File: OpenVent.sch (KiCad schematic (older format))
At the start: 0 parts

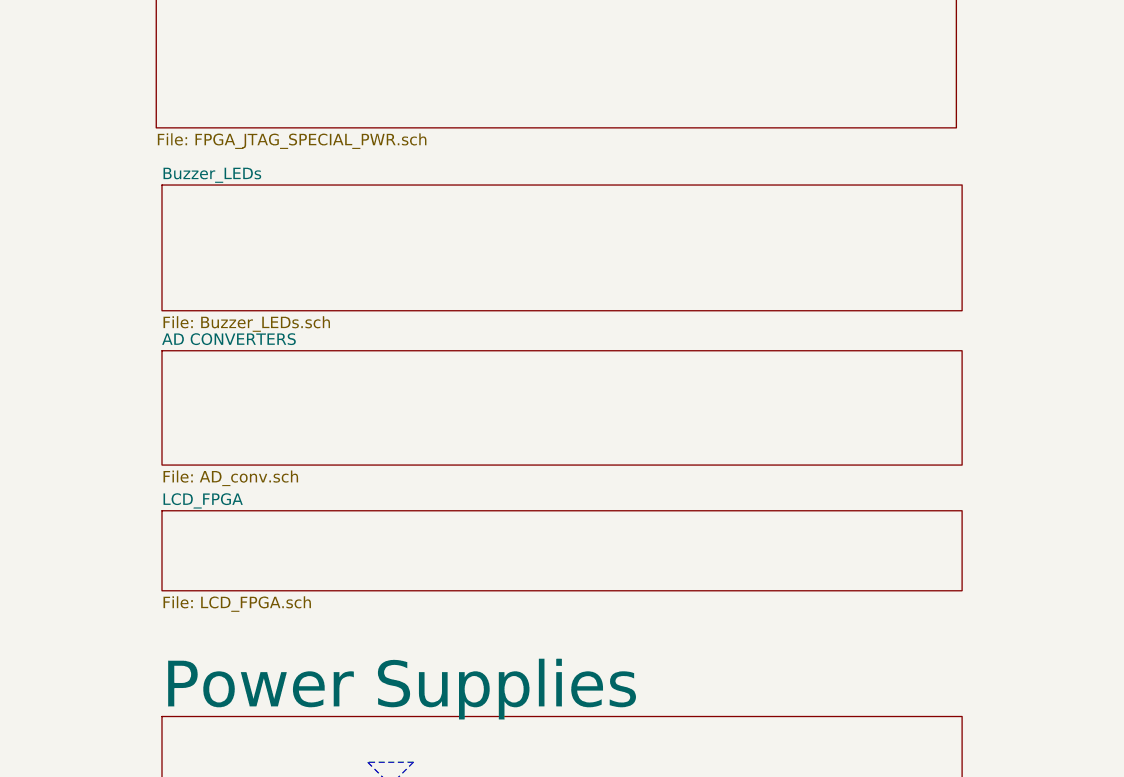
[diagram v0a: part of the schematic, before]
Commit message: Created UI sheet, changed membrance switch lable to push button
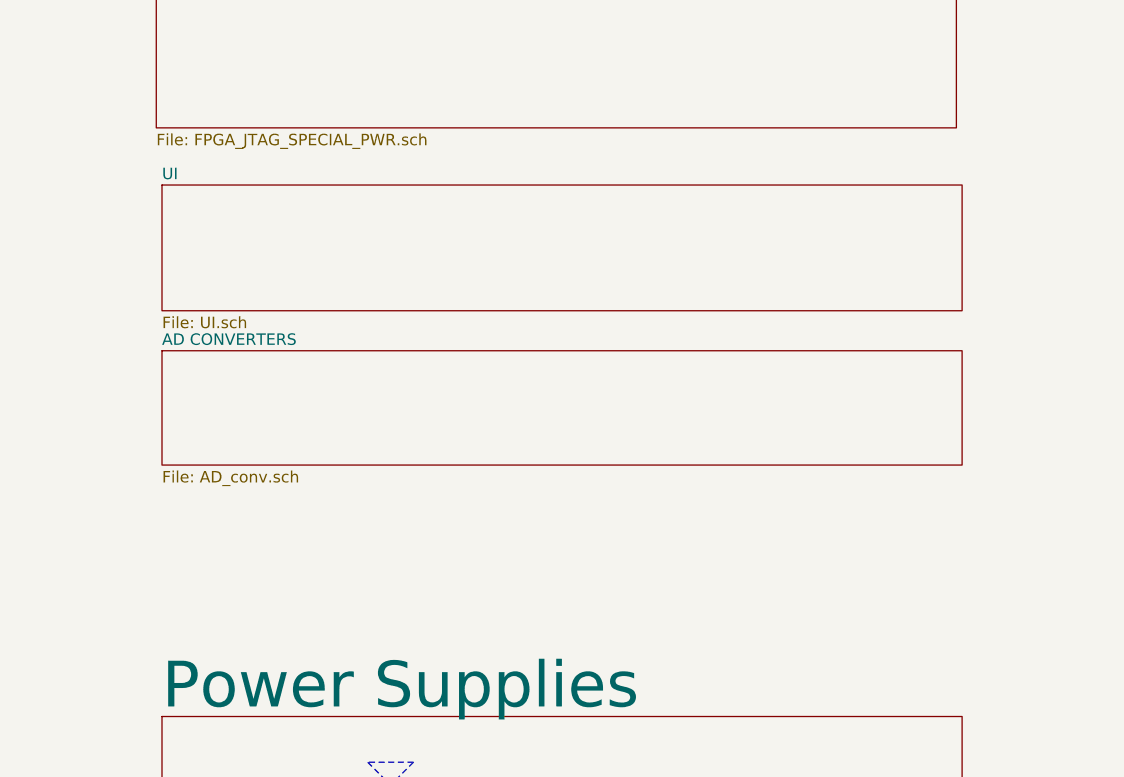
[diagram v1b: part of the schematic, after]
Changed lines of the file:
@@
 S 1500 2175 3500 550
 U 5FCA4074
-F0 "Buzzer_LEDs" 50
-F1 "Buzzer_LEDs.sch" 50
+F0 "UI" 50
+F1 "UI.sch" 50
 $EndSheet
 Text Notes 5775 200  0    50   ~ 0
@@
 F1 "AD_conv.sch" 50
 $EndSheet
-$Sheet
-S 1500 3600 3500 350
-U 601A5838
-F0 "LCD_FPGA" 50
-F1 "LCD_FPGA.sch" 50
-$EndSheet
 $EndSCHEMATC

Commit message: Swapped in Rick's front sheet. Note that this changed the sheet order, which appears to be automatically assigned and cannot be edited back to what it was manually
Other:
- note added: "+5V_Sensor"
- note added: "1V2"
- note added: "3V3"
- note added: "3V3-ALWAYS-ON"
- note added: "3V3_Sensor"
- note added: "7V5"
- note added: "Filter"
- note added: "KEYBD"
- note added: "LFT DISP"
- note added: "PB_Mute"
- note added: "RGT DISP"
- note added: "V_Main"
- note removed: "+3V3"
- note removed: "+3V3-ALWAYS-ON"
- note removed: "+5V_SENSE"
- note removed: "Display"
- note removed: "Key Pad"
- note removed: "VBATT IS 12V BUT CAN GO UP TO 14V"

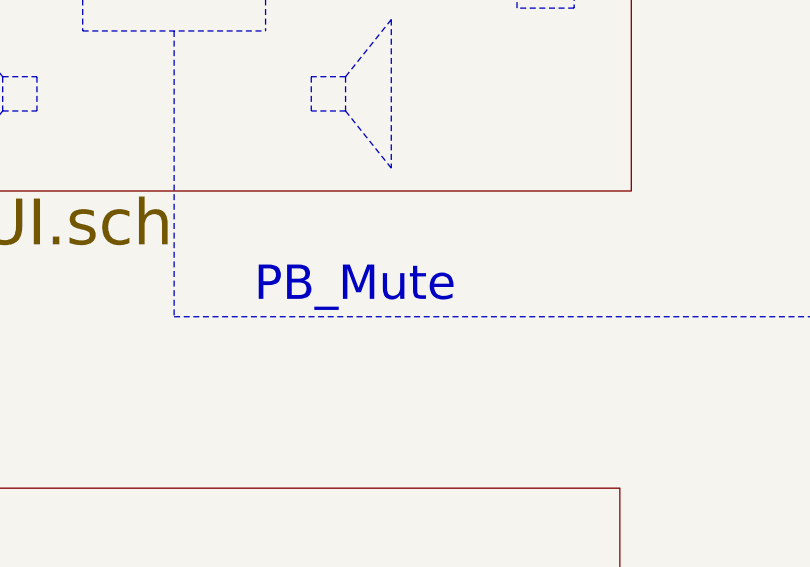
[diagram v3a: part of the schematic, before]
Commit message: Update OpenVent.sch
Main Sheet
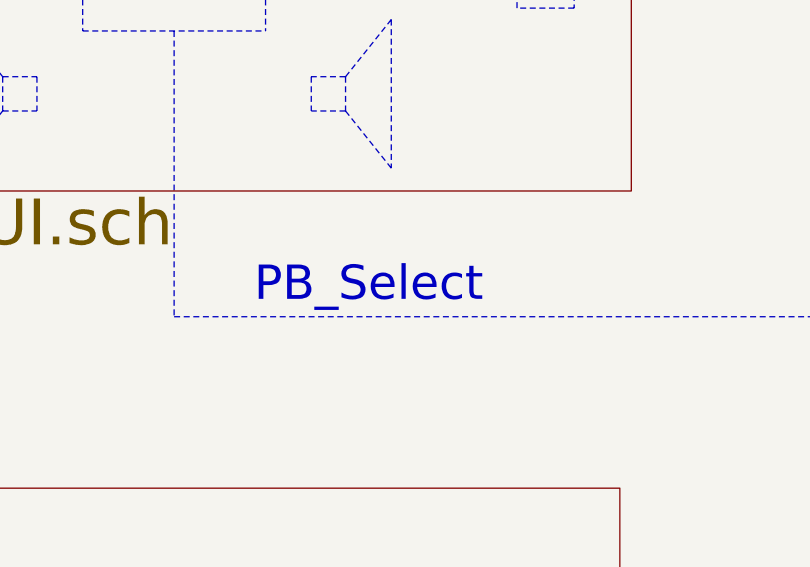
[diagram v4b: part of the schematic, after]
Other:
- note added: "PB_Select"
- note removed: "PB_Mute"
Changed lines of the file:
@@
 	3000 3100 3000 4350
 Text Notes 3350 4300 0    150  ~ 0
-PB_Mute
+PB_Select
 $EndSCHEMATC

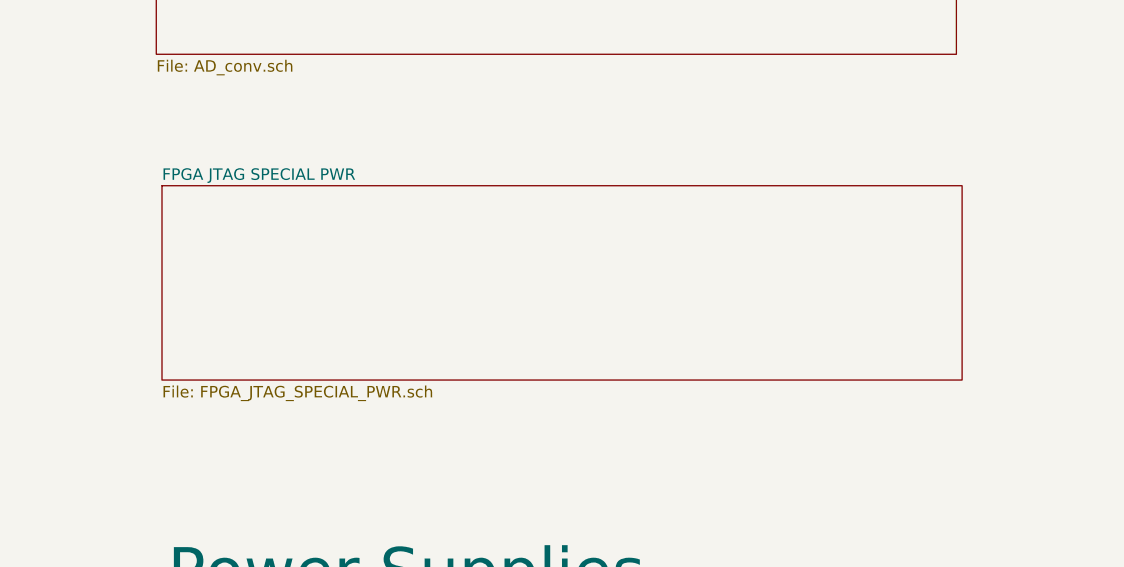
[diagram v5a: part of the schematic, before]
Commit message: Moved FPGA decoupling caps to FPGA sheet. Deleted FPGA JTAG SPECIAL PWR sheet as now empty
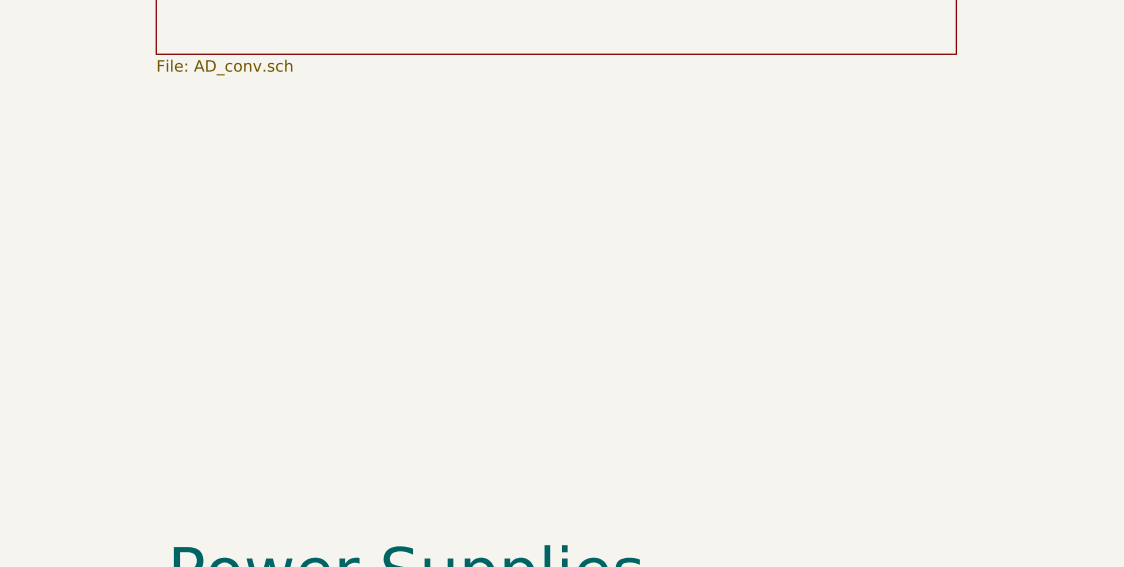
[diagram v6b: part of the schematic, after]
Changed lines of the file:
@@
 $Descr A3 16535 11693
 encoding utf-8
-Sheet 1 9
+Sheet 1 8
 Title "OpenVent Control Board"
 Date "2020-10-20"
@@
 	10900 9750 10900 10650
 Wire Notes Line style solid
+	15600 1400 15500 1500
+Wire Notes Line style solid
+	15500 1500 15600 1600
+Wire Notes Line style solid
+	15500 1400 15400 1500
+Wire Notes Line style solid
+	15400 1500 15500 1600
+Text Notes 15300 1350 0    150  ~ 0
+O2
+Wire Notes Line style solid
+	15700 1500 15500 1500
+Wire Notes Line style solid
+	13250 1500 15400 1500
+Wire Notes Line style solid
+	15600 2400 15500 2500
+Wire Notes Line style solid
+	15500 2500 15600 2600
+Wire Notes Line style solid
+	15500 2400 15400 2500
+Wire Notes Line style solid
+	15400 2500 15500 2600
+Text Notes 14800 2400 0    150  ~ 0
+Diff Press
+Wire Notes Line style solid
+	15700 2500 15500 2500
+Wire Notes Line style solid
+	9000 2500 15400 2500
+Wire Notes Line style solid
+	15600 2900 15500 3000
+Wire Notes Line style solid
+	15500 3000 15600 3100
+Wire Notes Line style solid
+	15500 2900 15400 3000
+Wire Notes Line style solid
+	15400 3000 15500 3100
+Text Notes 14800 2900 0    150  ~ 0
+Flow Press
+Wire Notes Line style solid
+	15700 3000 15500 3000
+Wire Notes Line style solid
+	15600 3400 15500 3500
+Wire Notes Line style solid
+	15500 3500 15600 3600
+Wire Notes Line style solid
+	15500 3400 15400 3500
+Wire Notes Line style solid
+	15400 3500 15500 3600
+Text Notes 14800 3400 0    150  ~ 0
+Pat Press
+Wire Notes Line style solid
+	15700 3500 15500 3500
+Wire Notes Line style solid
+	9000 3500 15400 3500
+Wire Notes Line style solid
+	13000 1500 13250 1650
+Wire Notes Line style solid
+	13250 1350 13000 1500
+Wire Notes Line style solid
+	13250 1350 13250 1650
+Wire Notes Line style solid
 	12700 1300 12800 1450
 Wire Notes Line style solid
@@
 	9000 1500 13000 1500
 Wire Notes Line style solid
+	13000 2000 13250 2150
+Wire Notes Line style solid
+	13250 1850 13000 2000
+Wire Notes Line style solid
 	12700 1800 12800 1950
 Wire Notes Line style solid
@@
 	9000 2000 13000 2000
 Wire Notes Line style solid
+	13250 1850 13250 2150
+Wire Notes Line style solid
+	13250 2000 13500 2000
+Wire Notes Line style solid
+	13250 3750 13250 3550
+Wire Notes Line style solid
+	13250 3650 13450 3650
+Wire Notes Line style solid
+	13200 3750 13200 3550
+Wire Notes Line style solid
+	13000 3650 13200 3650
+Wire Notes Line style solid
+	13400 3700 13500 3700
+Wire Notes Line style solid
+	13450 3750 13500 3700
+Wire Notes Line style solid
+	13450 3750 13400 3700
+Wire Notes Line style solid
+	13450 3700 13450 3650
+Wire Notes Line style solid
 	13000 3650 13000 3500
 Wire Notes Line style solid
+	13500 2500 13500 2000
+Wire Notes Line style solid
+	13250 3250 13250 3050
+Wire Notes Line style solid
+	13250 3150 13450 3150
+Wire Notes Line style solid
+	13200 3250 13200 3050
+Wire Notes Line style solid
+	13000 3150 13200 3150
+Wire Notes Line style solid
+	13400 3200 13500 3200
+Wire Notes Line style solid
+	13450 3250 13500 3200
+Wire Notes Line style solid
+	13450 3250 13400 3200
+Wire Notes Line style solid
+	13450 3200 13450 3150
+Wire Notes Line style solid
 	13000 3150 13000 3000
+Wire Notes Line style solid
+	13250 2750 13250 2550
+Wire Notes Line style solid
+	13250 2650 13450 2650
+Wire Notes Line style solid
+	13200 2750 13200 2550
+Wire Notes Line style solid
+	13000 2650 13200 2650
+Wire Notes Line style solid
+	13400 2700 13500 2700
+Wire Notes Line style solid
+	13450 2750 13500 2700
+Wire Notes Line style solid
+	13450 2750 13400 2700
+Wire Notes Line style solid
+	13450 2700 13450 2650
 Wire Notes Line style solid
 	13000 2650 13000 2500
 Text Notes 12650 2200 0    100  ~ 0
 4.65x
+$Sheet
+S 11000 1000 3500 2800
+U 5F8F3873
+F0 "Sensors" 200
+F1 "Sensors.sch" 200
+$EndSheet
 Wire Notes Line style solid
 	12000 9000 9000 9000
@@
 	9000 8100 9000 10500
 Wire Notes Line style solid
+	9000 3000 15400 3000
+Wire Notes Line style solid
 	7000 3700 9000 3700
 Wire Notes Line style solid
@@
 Text Notes 11350 7850 0    150  ~ 0
 JMPR
-$Sheet
-S 1475 6175 3500 850
-U 5FBE8499
-F0 "FPGA JTAG SPECIAL PWR" 50
-F1 "FPGA_JTAG_SPECIAL_PWR.sch" 50
-$EndSheet
 $Sheet
 S 1450 5100 3500 500
@@
 Text Notes 3350 4300 0    150  ~ 0
 PB_Select
-Wire Notes Line style solid
-	9000 3000 15400 3000
-$Sheet
-S 11000 1000 3500 2800
-U 5F8F3873
-F0 "Sensors" 200
-F1 "Sensors.sch" 200
-$EndSheet
-Wire Notes Line style solid
-	13450 2700 13450 2650
-Wire Notes Line style solid
-	13450 2750 13400 2700
-Wire Notes Line style solid
-	13450 2750 13500 2700
-Wire Notes Line style solid
-	13400 2700 13500 2700
-Wire Notes Line style solid
-	13000 2650 13200 2650
-Wire Notes Line style solid
-	13200 2750 13200 2550
-Wire Notes Line style solid
-	13250 2650 13450 2650
-Wire Notes Line style solid
-	13250 2750 13250 2550
-Wire Notes Line style solid
-	13450 3200 13450 3150
-Wire Notes Line style solid
-	13450 3250 13400 3200
-Wire Notes Line style solid
-	13450 3250 13500 3200
-Wire Notes Line style solid
-	13400 3200 13500 3200
-Wire Notes Line style solid
-	13000 3150 13200 3150
-Wire Notes Line style solid
-	13200 3250 13200 3050
-Wire Notes Line style solid
-	13250 3150 13450 3150
-Wire Notes Line style solid
-	13250 3250 13250 3050
-Wire Notes Line style solid
-	13500 2500 13500 2000
-Wire Notes Line style solid
-	13450 3700 13450 3650
-Wire Notes Line style solid
-	13450 3750 13400 3700
-Wire Notes Line style solid
-	13450 3750 13500 3700
-Wire Notes Line style solid
-	13400 3700 13500 3700
-Wire Notes Line style solid
-	13000 3650 13200 3650
-Wire Notes Line style solid
-	13200 3750 13200 3550
-Wire Notes Line style solid
-	13250 3650 13450 3650
-Wire Notes Line style solid
-	13250 3750 13250 3550
-Wire Notes Line style solid
-	13250 2000 13500 2000
-Wire Notes Line style solid
-	13250 1850 13250 2150
-Wire Notes Line style solid
-	13250 1850 13000 2000
-Wire Notes Line style solid
-	13000 2000 13250 2150
-Wire Notes Line style solid
-	13250 1350 13250 1650
-Wire Notes Line style solid
-	13250 1350 13000 1500
-Wire Notes Line style solid
-	13000 1500 13250 1650
-Wire Notes Line style solid
-	9000 3500 15400 3500
-Wire Notes Line style solid
-	15700 3500 15500 3500
-Text Notes 14800 3400 0    150  ~ 0
-Pat Press
-Wire Notes Line style solid
-	15400 3500 15500 3600
-Wire Notes Line style solid
-	15500 3400 15400 3500
-Wire Notes Line style solid
-	15500 3500 15600 3600
-Wire Notes Line style solid
-	15600 3400 15500 3500
-Wire Notes Line style solid
-	15700 3000 15500 3000
-Text Notes 14800 2900 0    150  ~ 0
-Flow Press
-Wire Notes Line style solid
-	15400 3000 15500 3100
-Wire Notes Line style solid
-	15500 2900 15400 3000
-Wire Notes Line style solid
-	15500 3000 15600 3100
-Wire Notes Line style solid
-	15600 2900 15500 3000
-Wire Notes Line style solid
-	9000 2500 15400 2500
-Wire Notes Line style solid
-	15700 2500 15500 2500
-Text Notes 14800 2400 0    150  ~ 0
-Diff Press
-Wire Notes Line style solid
-	15400 2500 15500 2600
-Wire Notes Line style solid
-	15500 2400 15400 2500
-Wire Notes Line style solid
-	15500 2500 15600 2600
-Wire Notes Line style solid
-	15600 2400 15500 2500
-Wire Notes Line style solid
-	13250 1500 15400 1500
-Wire Notes Line style solid
-	15700 1500 15500 1500
-Text Notes 15300 1350 0    150  ~ 0
-O2
-Wire Notes Line style solid
-	15400 1500 15500 1600
-Wire Notes Line style solid
-	15500 1400 15400 1500
-Wire Notes Line style solid
-	15500 1500 15600 1600
-Wire Notes Line style solid
-	15600 1400 15500 1500
 $EndSCHEMATC
